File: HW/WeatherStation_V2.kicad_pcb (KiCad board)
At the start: 2 copper layers, 74.9 x 61 mm, 61 parts, among them J1 Sensors + PWR, J10 BATTERY, J2 I2C, J3 DHT, J4 I2C, J5 GPIO2, J6 I2C, J7 I2C, J9 PROG, Q1 BC817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

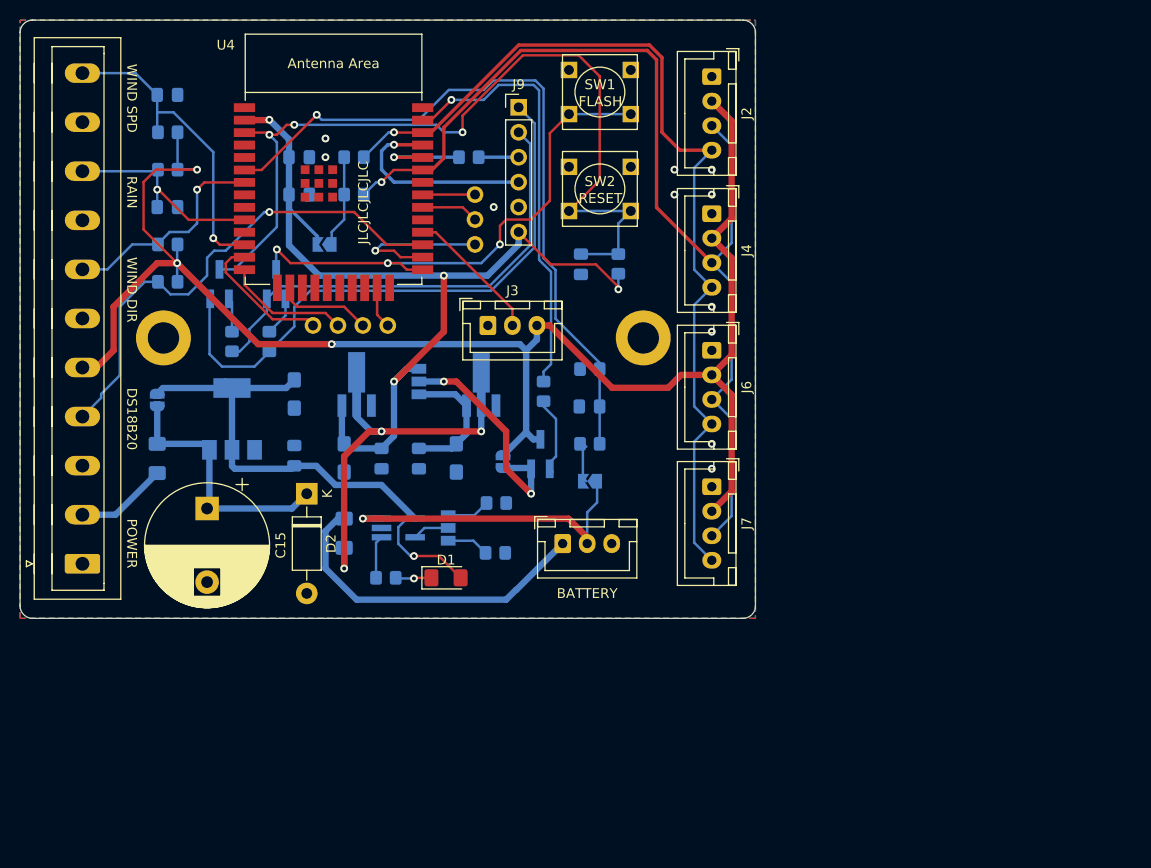
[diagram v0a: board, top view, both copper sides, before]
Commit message: Updated PCB - DRC OK
DRC without any error;
some small improvements in scheme
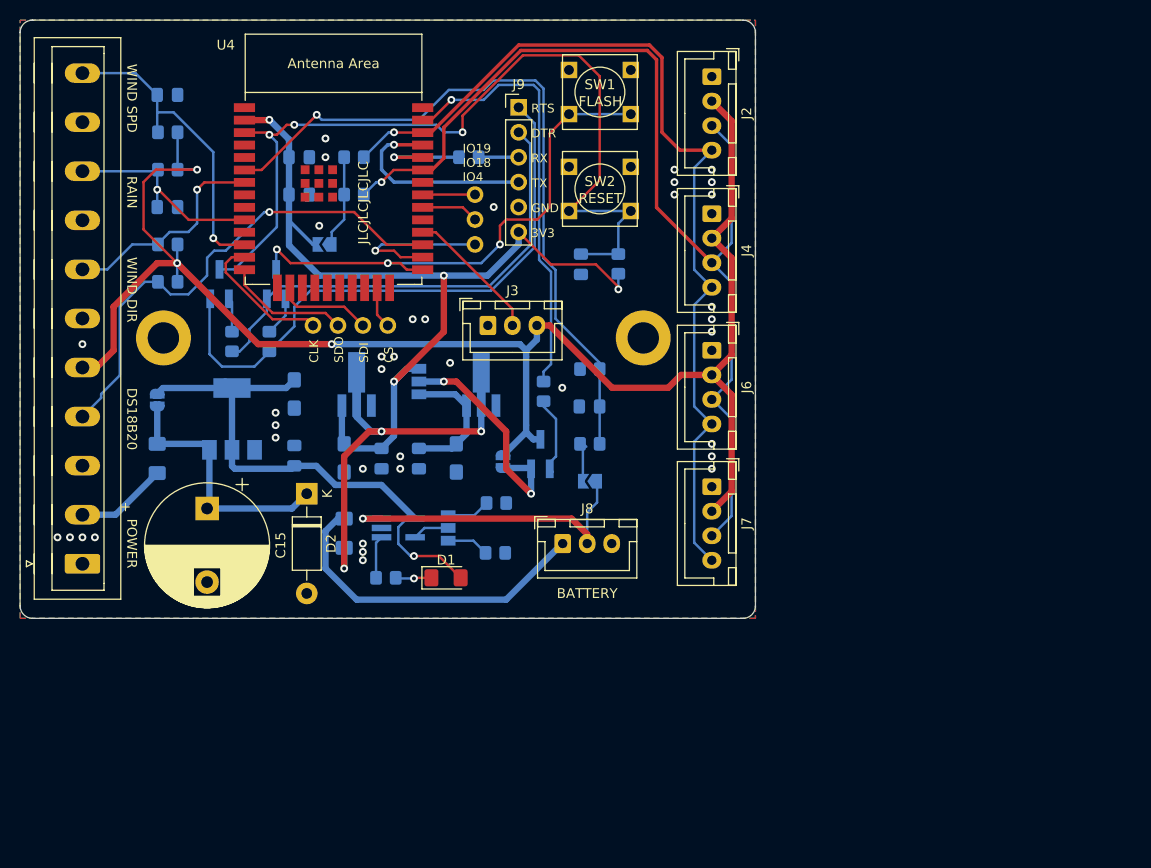
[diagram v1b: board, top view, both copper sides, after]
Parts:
- removed J10: BATTERY, Connector_JST:JST_XH_B3B-XH-A_1x03_P2.50mm_Vertical
- added J8: BATTERY, Connector_JST:JST_XH_B3B-XH-A_1x03_P2.50mm_Vertical, F.Cu at (132.8, 106.7)
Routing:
- net GND: vias 11 -> 37
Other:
- board text added: "+"
- board text added: "3V3"
- board text added: "CLK"
- board text added: "CS"
- board text added: "DTR"
- board text added: "GND"
- board text added: "IO19 IO18 IO4"
- board text added: "RTS"
- board text added: "RX"
- board text added: "SDI"
- board text added: "SDO"
- board text added: "TX"

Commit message: small improvements
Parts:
- moved C1 44.7 mm to (152.4, 121.5)
- moved C14 44.7 mm to (156.2, 121.5)
- moved H2 44.7 mm to (130.2, 109.2)
- moved J1 44.7 mm to (121.9, 132.2)
- moved C10 44.7 mm to (160.0, 121.4)
- moved C13 44.7 mm to (173.6, 116.1)
- moved C15 44.7 mm to (134.6, 126.5)
- moved C7 44.7 mm to (148.6, 121.4)
- moved C8 44.7 mm to (143.5, 121.2)
- moved D2 44.7 mm to (144.8, 125.0)
- moved F1 44.7 mm to (129.5, 121.4)
- moved F2 44.7 mm to (148.6, 129.1)
- moved GPIO1 44.7 mm to (161.9, 99.6)
- moved H1 44.7 mm to (179.1, 109.2)
- moved J3 44.7 mm to (163.2, 107.9)
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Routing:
- net GND: vias 37 -> 36

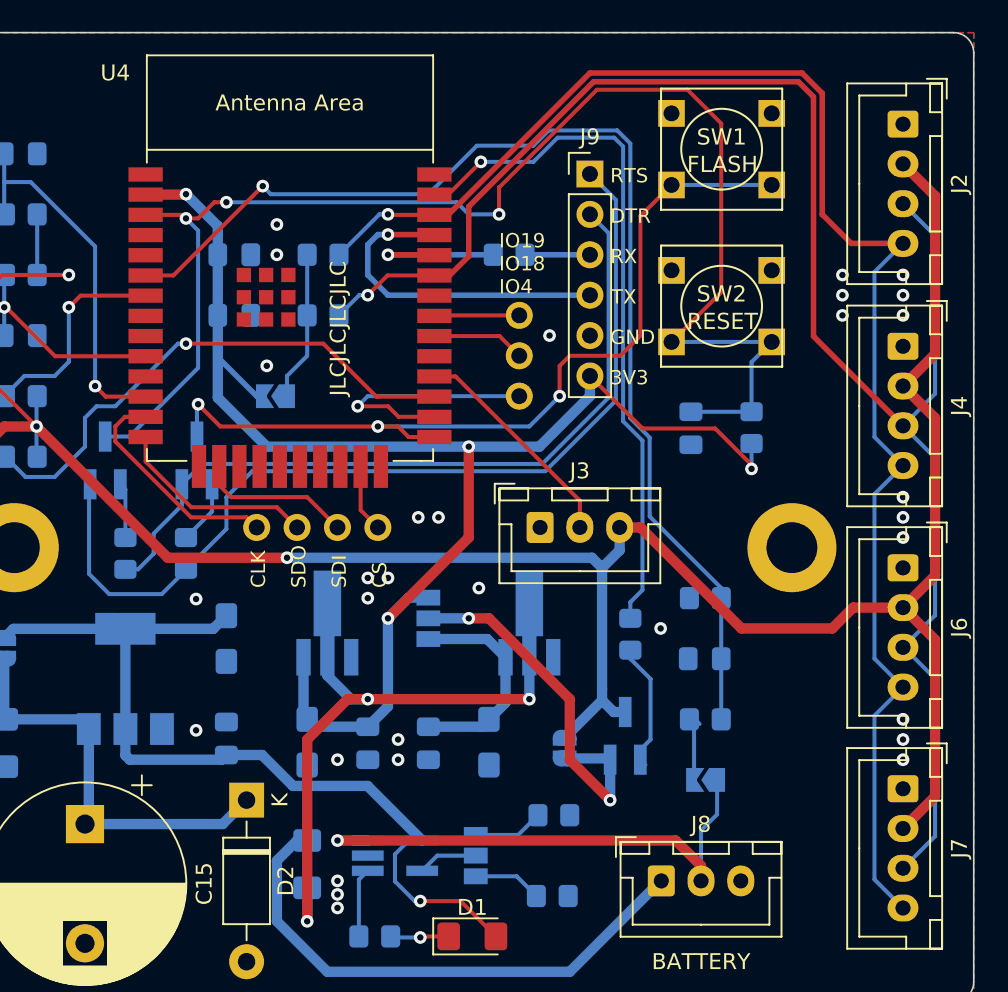
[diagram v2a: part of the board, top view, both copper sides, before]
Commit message: added keepout area
Updated antenna area - added keepout area

Updated text on Silkscreen layer
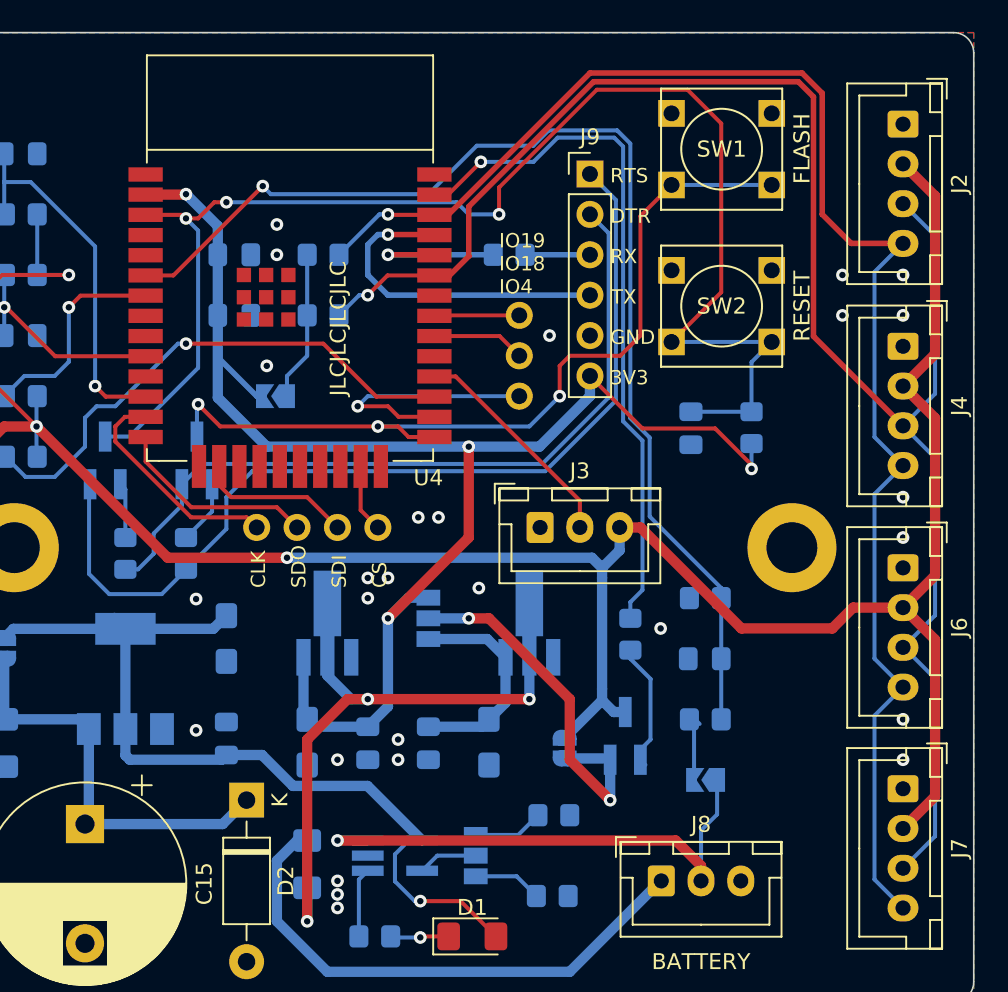
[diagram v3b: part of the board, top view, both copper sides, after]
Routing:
- net GND: vias 36 -> 32
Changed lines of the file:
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@@
     (property "ki_keywords" "ESP32")
     (attr smd)
-    (fp_text reference "U4" (at -10.985 -13.39) (layer "F.SilkS")
+    (fp_text reference "U4" (at 8.7 12.066036) (layer "F.SilkS")
         (effects (font (size 1 1) (thickness 0.15)))
     )
@@
         (effects (font (size 1 1) (thickness 0.15)))
     )
-    (fp_text user "Antenna Area" (at 0 -11.5) (layer "F.SilkS")
-        (effects (font (size 1 1) (thickness 0.15)))
-    )
-    (fp_text user "Antenna Area" (at 0 -11.5) (layer "Eco2.User")
-        (effects (font (size 1 1) (thickness 0.15)))
-    )
     (fp_text user "${REFERENCE}" (at 0 0) (layer "F.Fab")
         (effects (font (size 1 1) (thickness 0.15)))
@@
     (fp_line (start 7.45 3.4) (end 7.45 -2.35)
       (stroke (width 0.1) (type solid)) (layer "F.Fab"))
-    (pad "1" thru_hole roundrect (at 0 0) (size 1.7 1.95) (drill 0.95) (layers "*.Cu" "*.Mask") (roundrect_rratio 0.147059)
+    (pad "1" thru_hole roundrect (at 0 0) (size 1.7 1.95) (drill 0.95) (layers "*.Cu" "*.Mask") (roundrect_rratio 0.1470588235)
       (net 49 "Net-(J8-Pin_1)") (pinfunction "Pin_1") (pintype "passive"))
     (pad "2" thru_hole oval (at 2.5 0) (size 1.7 1.95) (drill 0.95) (layers "*.Cu" "*.Mask")
@@
     (fp_line (start 9.95 3.4) (end 9.95 -2.35)
       (stroke (width 0.1) (type solid)) (layer "F.Fab"))
-    (pad "1" thru_hole roundrect (at 0 0 270) (size 1.7 1.95) (drill 0.95) (layers "*.Cu" "*.Mask") (roundrect_rratio 0.147059)
+    (pad "1" thru_hole roundrect (at 0 0 270) (size 1.7 1.95) (drill 0.95) (layers "*.Cu" "*.Mask") (roundrect_rratio 0.1470588235)
       (net 2 "GND") (pinfunction "Pin_1") (pintype "passive"))
     (pad "2" thru_hole oval (at 2.5 0 270) (size 1.7 1.95) (drill 0.95) (layers "*.Cu" "*.Mask")
@@
     (fp_line (start 9.95 3.4) (end 9.95 -2.35)
       (stroke (width 0.1) (type solid)) (layer "F.Fab"))
-    (pad "1" thru_hole roundrect (at 0 0 270) (size 1.7 1.95) (drill 0.95) (layers "*.Cu" "*.Mask") (roundrect_rratio 0.147059)
+    (pad "1" thru_hole roundrect (at 0 0 270) (size 1.7 1.95) (drill 0.95) (layers "*.Cu" "*.Mask") (roundrect_rratio 0.1470588235)
       (net 2 "GND") (pinfunction "Pin_1") (pintype "passive"))
     (pad "2" thru_hole oval (at 2.5 0 270) (size 1.7 1.95) (drill 0.95) (layers "*.Cu" "*.Mask")
@@
     (property "ki_keywords" "switch normally-open pushbutton push-button")
     (attr through_hole)
-    (fp_text reference "SW2" (at 0 -0.762) (layer "F.SilkS")
+    (fp_text reference "SW2" (at 0 0) (layer "F.SilkS")
         (effects (font (size 1.016 1.016) (thickness 0.2032)))
     )
-    (fp_text value "RESET" (at 0.0508 0.9652 180) (layer "F.SilkS")
+    (fp_text value "RESET" (at 5.055 0.001036 -90) (layer "F.SilkS")
         (effects (font (size 1.016 1.016) (thickness 0.2032)))
     )
@@
     (fp_line (start 9.95 3.4) (end 9.95 -2.35)
       (stroke (width 0.1) (type solid)) (layer "F.Fab"))
-    (pad "1" thru_hole roundrect (at 0 0 270) (size 1.7 1.95) (drill 0.95) (layers "*.Cu" "*.Mask") (roundrect_rratio 0.147059)
+    (pad "1" thru_hole roundrect (at 0 0 270) (size 1.7 1.95) (drill 0.95) (layers "*.Cu" "*.Mask") (roundrect_rratio 0.1470588235)
       (net 2 "GND") (pinfunction "Pin_1") (pintype "passive"))
     (pad "2" thru_hole oval (at 2.5 0 270) (size 1.7 1.95) (drill 0.95) (layers "*.Cu" "*.Mask")
@@
     (property "ki_keywords" "switch normally-open pushbutton push-button")
     (attr through_hole)
-    (fp_text reference "SW1" (at 0 -0.762) (layer "F.SilkS")
+    (fp_text reference "SW1" (at 0 0) (layer "F.SilkS")
         (effects (font (size 1.016 1.016) (thickness 0.2032)))
     )
-    (fp_text value "FLASH" (at 0.0508 0.9652 180) (layer "F.SilkS")
+    (fp_text value "FLASH" (at 5.055 -0.034964 -90) (layer "F.SilkS")
         (effects (font (size 1.016 1.016) (thickness 0.2032)))
     )
@@
     (fp_line (start 9.95 3.4) (end 9.95 -2.35)
       (stroke (width 0.1) (type solid)) (layer "F.Fab"))
-    (pad "1" thru_hole roundrect (at 0 0 270) (size 1.7 1.95) (drill 0.95) (layers "*.Cu" "*.Mask") (roundrect_rratio 0.147059)
+    (pad "1" thru_hole roundrect (at 0 0 270) (size 1.7 1.95) (drill 0.95) (layers "*.Cu" "*.Mask") (roundrect_rratio 0.1470588235)
       (net 2 "GND") (pinfunction "Pin_1") (pintype "passive"))
     (pad "2" thru_hole oval (at 2.5 0 270) (size 1.7 1.95) (drill 0.95) (layers "*.Cu" "*.Mask")
@@
     (property "ki_keywords" "solder jumper SPST")
     (attr exclude_from_pos_files)
-    (fp_text reference "JP2" (at 0 1.905 90) (layer "B.SilkS")
+    (fp_text reference "JP2" (at -0.071036 -1.905 270) (layer "B.SilkS")
         (effects (font (size 1 1) (thickness 0.15)) (justify mirror))
     )
@@
   (via (at 146.05 97.733964) (size 0.8) (drill 0.4) (layers "F.Cu" "B.Cu") (free) (net 2))
   (via (at 186.055 105.988964) (size 0.8) (drill 0.4) (layers "F.Cu" "B.Cu") (free) (net 2))
-  (via (at 186.055 121.228964) (size 0.8) (drill 0.4) (layers "F.Cu" "B.Cu") (free) (net 2))
   (via (at 182.245 94.558964) (size 0.8) (drill 0.4) (layers "F.Cu" "B.Cu") (free) (net 2))
   (via (at 163.83 95.828964) (size 0.8) (drill 0.4) (layers "F.Cu" "B.Cu") (free) (net 2))
@@
   (via (at 150.495 130.118964) (size 0.8) (drill 0.4) (layers "F.Cu" "B.Cu") (free) (net 2))
   (via (at 186.055 94.558964) (size 0.8) (drill 0.4) (layers "F.Cu" "B.Cu") (free) (net 2))
-  (via (at 186.055 93.288964) (size 0.8) (drill 0.4) (layers "F.Cu" "B.Cu") (free) (net 2))
   (via (at 141.605 120.65) (size 0.8) (drill 0.4) (layers "F.Cu" "B.Cu") (free) (net 2))
   (via (at 152.4 111.068964) (size 0.8) (drill 0.4) (layers "F.Cu" "B.Cu") (free) (net 2))
@@
   (via (at 146.685 90.748964) (size 0.8) (drill 0.4) (layers "F.Cu" "B.Cu") (free) (net 2))
   (via (at 146.685 88.843964) (size 0.8) (drill 0.4) (layers "F.Cu" "B.Cu") (free) (net 2))
-  (via (at 186.055 107.258964) (size 0.8) (drill 0.4) (layers "F.Cu" "B.Cu") (free) (net 2))
   (via (at 153.67 111.068964) (size 0.8) (drill 0.4) (layers "F.Cu" "B.Cu") (free) (net 2))
   (via (at 186.055 122.498964) (size 0.8) (drill 0.4) (layers "F.Cu" "B.Cu") (free) (net 2))
@@
   (via (at 156.845 107.258964) (size 0.8) (drill 0.4) (layers "F.Cu" "B.Cu") (free) (net 2))
   (via (at 150.495 122.498964) (size 0.8) (drill 0.4) (layers "F.Cu" "B.Cu") (free) (net 2))
-  (via (at 182.245 93.288964) (size 0.8) (drill 0.4) (layers "F.Cu" "B.Cu") (free) (net 2))
   (segment (start 172.899882 112.413964) (end 172.974882 112.338964) (width 0.254) (layer "B.Cu") (net 2))
   (segment (start 176.53 104.210964) (end 176.53 103.956964) (width 0.254) (layer "F.Cu") (net 3))
@@
       )
     )
+  )
+  (zone (net 0) (net_name "") (layers "F&B.Cu") (hatch edge 0.5)
+    (connect_pads (clearance 0))
+    (min_thickness 0.25) (filled_areas_thickness no)
+    (keepout (tracks not_allowed) (vias not_allowed) (pads not_allowed) (copperpour not_allowed) (footprints allowed))
+    (fill (thermal_gap 0.5) (thermal_bridge_width 0.5))
+    (polygon
+      (pts
+        (xy 158.2 76.835)
+        (xy 158.2 84.2)
+        (xy 136.8 84.2)
+        (xy 136.8 76.8)
+      )
+    )

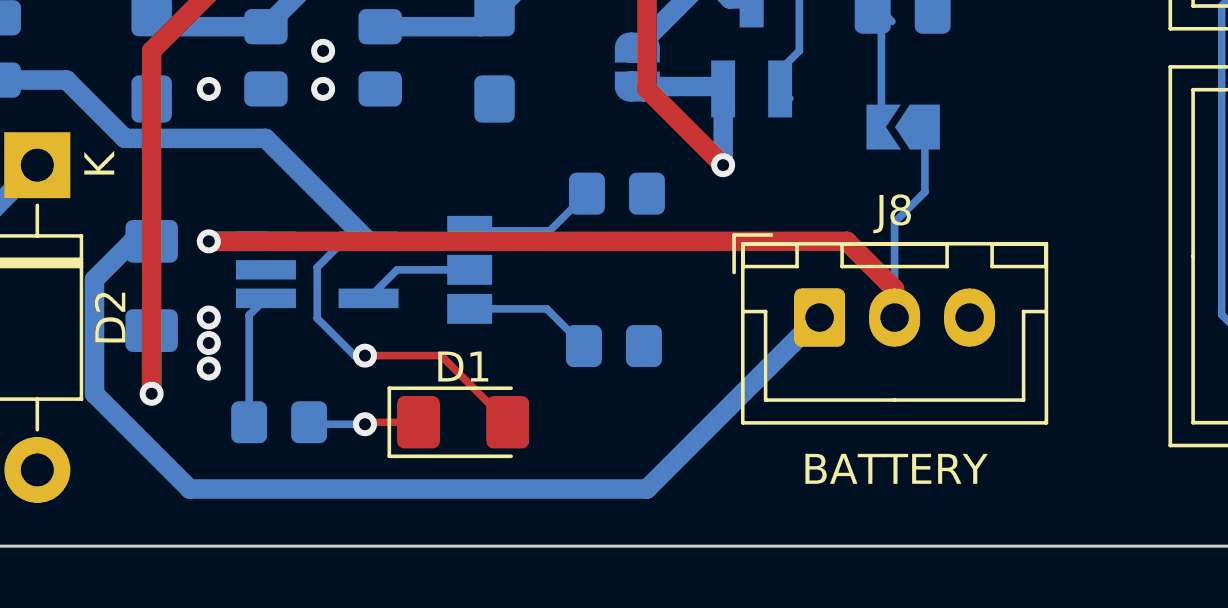
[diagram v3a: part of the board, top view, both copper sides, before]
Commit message: 3 pin battery connector updated to 2 pin
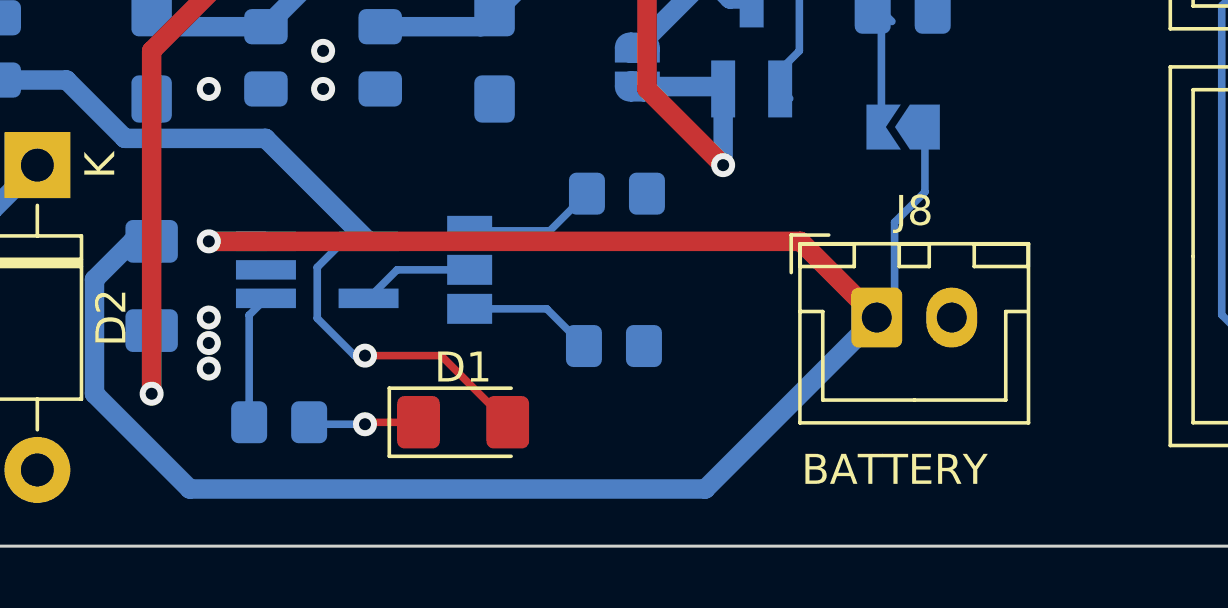
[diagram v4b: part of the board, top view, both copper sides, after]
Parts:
- J8: footprint Connector_JST:JST_XH_B3B-XH-A_1x03_P2.50mm_Vertical -> Connector_JST:JST_XH_B2B-XH-A_1x02_P2.50mm_Vertical
- moved J8 1.91 mm to (172.8, 130.1)
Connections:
- F2 pad 1: Net-(J8-Pin_1) -> +BATT
- J8 pad 1: Net-(J8-Pin_1) -> +BATT
- J8 pad 2: +BATT -> GND
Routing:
- net +BATT: track 33.1 -> 68.0 mm
- net Net-(J8-Pin_1): track 34.1 -> 0.00 mm
